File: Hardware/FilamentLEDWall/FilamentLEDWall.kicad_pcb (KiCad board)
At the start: 2 copper layers, 23 parts, among them U1 AMS1117-3.3, U2 AMS1117-5.0, U3 JXI5020GF

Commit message: updated circuit
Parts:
- removed C2: 10uF, Capacitor_SMD:C_0805_2012Metric_Pad1.15x1.40mm_HandSolder
- removed MOD1: ESP32-WROOM-32, digikey-footprints:ESP32-WROOM-32D
- removed U1: AMS1117-3.3, Package_TO_SOT_SMD:SOT-223-3_TabPin2
- removed U2: AMS1117-5.0, Package_TO_SOT_SMD:SOT-223-3_TabPin2
- added J1: TopLeftConnector, Connector_PinHeader_2.54mm:PinHeader_2x04_P2.54mm_Vertical_SMD, B.Cu at (81.8, 40.0)
- added J2: TopLeftConnector, Connector_PinHeader_2.54mm:PinHeader_2x04_P2.54mm_Vertical_SMD, B.Cu at (81.8, 145.0)
- added J3: TopLeftConnector, Connector_PinHeader_2.54mm:PinHeader_2x04_P2.54mm_Vertical_SMD, B.Cu at (186.8, 145.0)
- added J4: TopLeftConnector, Connector_PinHeader_2.54mm:PinHeader_2x04_P2.54mm_Vertical_SMD, B.Cu at (186.8, 40.0)
- C1, R1, U3: moved to B.Cu
- D1, D10, D11, D12, D13, D14, D15, D16, D2, D3, D4, D5, D6, D7, D8, D9: footprint LED_SMD:LED_0805_2012Metric_Pad1.15x1.40mm_HandSolder -> FilamentLEDWall:FilamentLED_30mm
- moved D13 104.1 mm to (90.8, 136.0), turned to 315 degrees
- moved D9 93.4 mm to (90.8, 107.0), turned to 225 degrees
- moved D15 69.0 mm to (148.8, 136.0), turned to 315 degrees
- moved D1 65.8 mm to (90.8, 49.0), turned to 225 degrees
- moved D5 64.2 mm to (90.8, 78.0), turned to 315 degrees
- moved D16 62.4 mm to (177.8, 136.0), turned to 45 degrees
- moved D14 58.0 mm to (119.8, 136.0), turned to 45 degrees
- moved R1 46.1 mm to (132.2, 87.0)
- moved D2 45.4 mm to (119.8, 49.0), turned to 135 degrees
- moved D12 41.9 mm to (177.8, 107.0), turned to 135 degrees
- moved D10 41.7 mm to (119.8, 107.0), turned to 135 degrees
- moved D6 41.5 mm to (119.8, 78.0), turned to 45 degrees
- moved D4 38.2 mm to (177.8, 49.0), turned to 135 degrees
- moved U3 35.2 mm to (134.2, 92.5), turned to 270 degrees
- moved D11 32.9 mm to (148.8, 107.0), turned to 225 degrees
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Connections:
- C1 pad 1: /3.3V_MCU -> /5V_LED
- U3 pad 22: (no net) -> LED_SDO
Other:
- board outline added: 116 x 116 mm
- rule pad_to_mask_clearance: 0.051 -> 0.05

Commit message: Updated light PCB v0.1
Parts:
- added C2: 100nF, Capacitor_SMD:C_0603_1608Metric_Pad1.05x0.95mm_HandSolder, B.Cu at (110.8, 67.1)
- C1: footprint Capacitor_SMD:C_0805_2012Metric_Pad1.15x1.40mm_HandSolder -> Capacitor_SMD:C_0603_1608Metric_Pad1.05x0.95mm_HandSolder
- J2: value TopLeftConnector -> BottomLeftConnector
- J3: value TopLeftConnector -> BottomRightConnector
- J4: value TopLeftConnector -> TopRightConnector
- R1: footprint Resistor_SMD:R_0805_2012Metric_Pad1.15x1.40mm_HandSolder -> Resistor_SMD:R_0603_1608Metric_Pad1.05x0.95mm_HandSolder
- moved U3 34.2 mm to (116.5, 63.3), turned to 0 degrees
- moved C1 30.8 mm to (110.8, 69.6), turned to 180 degrees
- moved J3 26.3 mm to (164.7, 130.6), turned to 180 degrees
- moved R1 25.7 mm to (113.3, 69.6), turned to 270 degrees
- moved D16 24.4 mm to (157.1, 123.0)
- moved D12 23.9 mm to (157.1, 95.0)
- moved J4 23.6 mm to (164.7, 31.5), turned to 270 degrees
- moved D15 23.5 mm to (129.2, 123.0)
- moved D8 23.3 mm to (157.1, 67.1)
- moved D11 22.9 mm to (129.2, 95.0)
- moved D4 22.9 mm to (157.1, 39.2)
- moved D14 22.6 mm to (101.2, 123.0)
- moved D7 22.4 mm to (129.2, 67.1)
- moved D10 22.0 mm to (101.2, 95.0)
- moved D3 21.9 mm to (129.2, 39.2)
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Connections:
- D1 pad 2: 5V -> /5V_LED
- D10 pad 2: 5V -> /5V_LED
- D11 pad 2: 5V -> /5V_LED
- D12 pad 2: 5V -> /5V_LED
- D13 pad 2: 5V -> /5V_LED
- D14 pad 2: 5V -> /5V_LED
- D15 pad 2: 5V -> /5V_LED
- D16 pad 2: 5V -> /5V_LED
- D2 pad 2: 5V -> /5V_LED
- D3 pad 2: 5V -> /5V_LED
- D4 pad 2: 5V -> /5V_LED
- D5 pad 2: 5V -> /5V_LED
- D6 pad 2: 5V -> /5V_LED
- D7 pad 2: 5V -> /5V_LED
- D8 pad 2: 5V -> /5V_LED
- D9 pad 2: 5V -> /5V_LED
- J1 pad 2: LED_CLK -> /5V_LED
- J1 pad 3: LED_LE -> LED_CLK
- J1 pad 4: LED_OE -> (no net)
- J1 pad 5: GND -> LED_LE
- J1 pad 7: LED_SDI -> LED_OE
- J1 pad 8: /5V_LED -> GND
- J2 pad 2: LED_CLK -> /5V_LED
- J2 pad 3: LED_LE -> LED_CLK
- J2 pad 4: LED_OE -> LED_SDI
- J2 pad 5: GND -> LED_LE
- J2 pad 6: LED_SDO -> (no net)
- J2 pad 7: LED_SDI -> LED_OE
- J2 pad 8: /5V_LED -> GND
- J3 pad 2: LED_CLK -> /5V_LED
- J3 pad 3: LED_LE -> LED_CLK
- J3 pad 4: LED_OE -> (no net)
- J3 pad 5: GND -> LED_LE
- J3 pad 7: LED_SDI -> LED_OE
- J3 pad 8: /5V_LED -> GND
- J4 pad 2: LED_CLK -> /5V_LED
- J4 pad 3: LED_LE -> LED_CLK
- J4 pad 4: LED_OE -> LED_SDI
- J4 pad 5: GND -> LED_LE
- J4 pad 6: LED_SDO -> (no net)
- J4 pad 7: LED_SDI -> LED_OE
- J4 pad 8: /5V_LED -> GND
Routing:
- net /5V_LED: track 0.00 -> 383.3 mm, vias 0 -> 2
- net LED_OE: track 0.00 -> 334.6 mm, vias 0 -> 18
- net LED_LE: track 0.00 -> 322.7 mm, vias 0 -> 16
- net LED_CLK: track 0.00 -> 317.5 mm, vias 0 -> 16
- net LED_SDI: track 0.00 -> 202.6 mm, vias 0 -> 14
- net LED_SDO: track 0.00 -> 195.4 mm, vias 0 -> 11
- net OUT12: track 0.00 -> 123.7 mm, vias 0 -> 2
- net OUT15: track 0.00 -> 120.5 mm, vias 0 -> 4
- net OUT0: track 0.00 -> 86.1 mm, vias 0 -> 2
- net OUT3: track 0.00 -> 84.3 mm, vias 0 -> 2
- net OUT8: track 0.00 -> 73.8 mm, vias 0 -> 4
- net OUT13: track 0.00 -> 72.4 mm, vias 0 -> 4
- net OUT14: track 0.00 -> 71.7 mm, vias 0 -> 4
- net OUT4: track 0.00 -> 70.5 mm, vias 0 -> 2
- net OUT11: track 0.00 -> 67.4 mm, vias 0 -> 2
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- added copper zone on B.Cu, net GND
- added copper zone on F.Cu, net GND
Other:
- board size 116 x 116 mm -> 113.8 x 113.8 mm
- board text added: "100nF"
- board text added: "10uF"
- board text added: "Filament Wall Cell v0.1 Sandbox Workshop Designed by Caorx Wangyw"
- board text added: "INPUT"
- board text added: "Iout=Vext(1.24V)/Rext*15"
- board text added: "OUTPUT"
- board text added: "R_EXT"

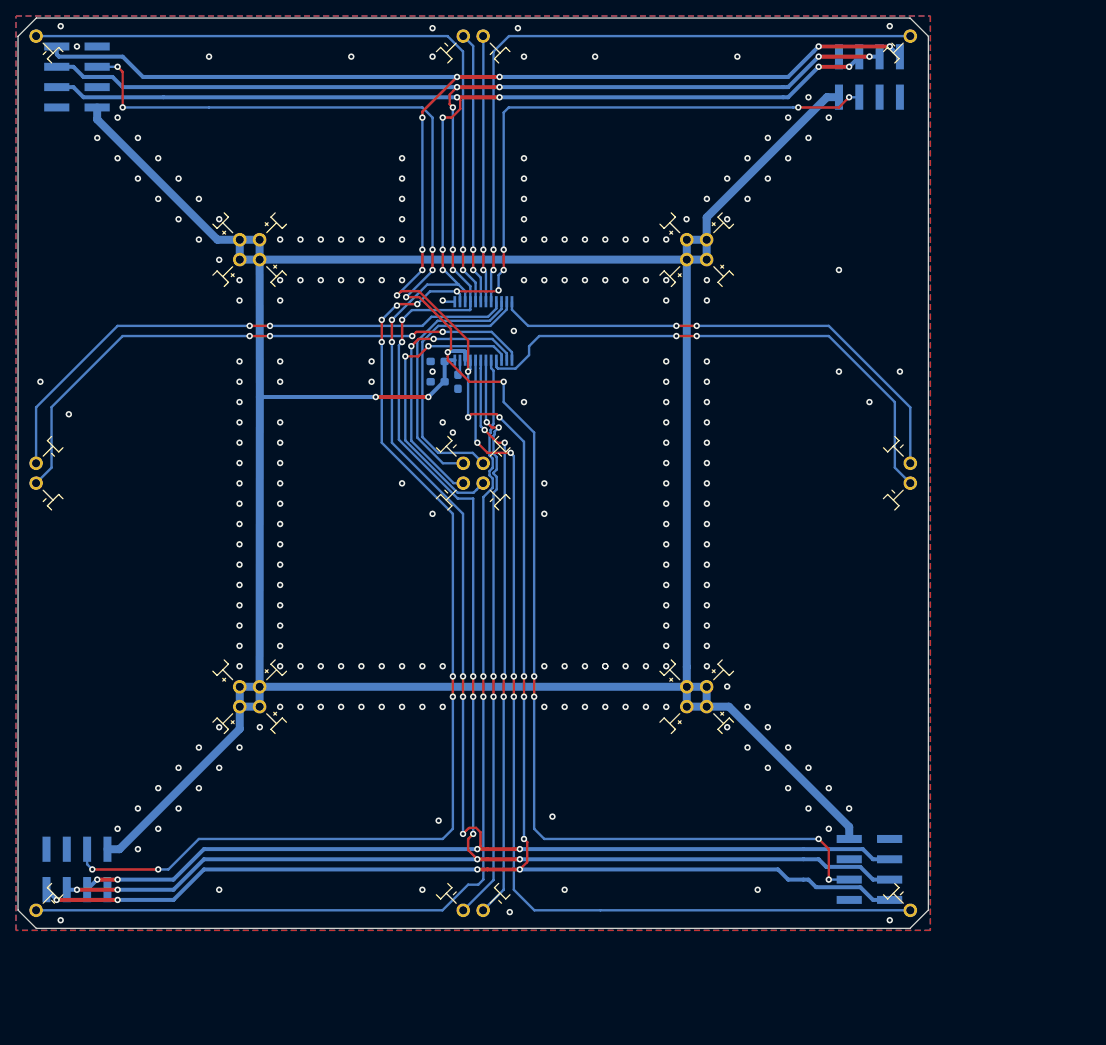
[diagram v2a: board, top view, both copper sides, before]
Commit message: Updated LED Board to v0.2
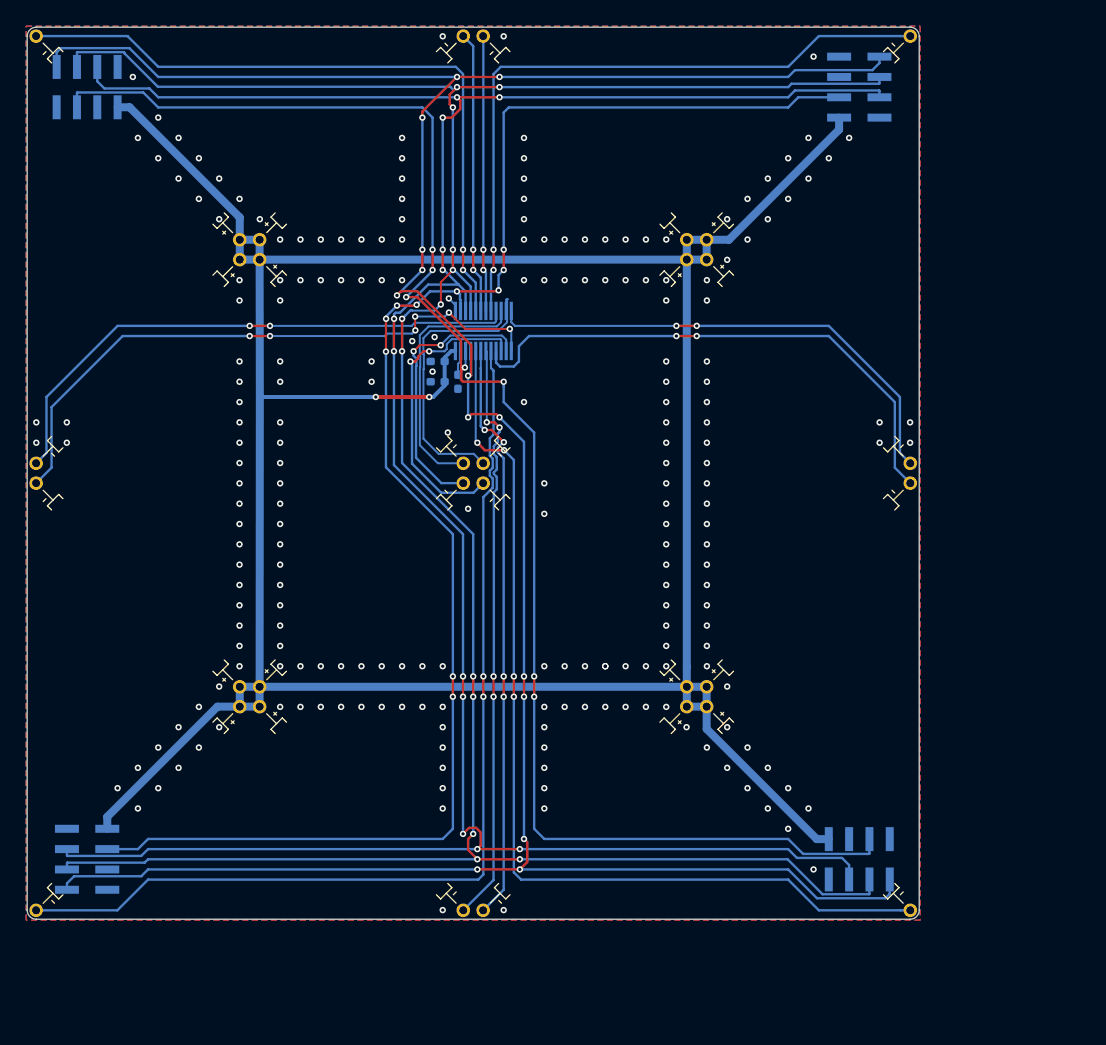
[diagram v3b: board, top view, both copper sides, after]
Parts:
- J1, J2, J3, J4: footprint Connector_PinHeader_2.54mm:PinHeader_2x04_P2.54mm_Vertical_SMD -> Connector_PinSocket_2.54mm:PinSocket_2x04_P2.54mm_Vertical_SMD
- U3: footprint Silicon-Standard:SSOP24 -> Sensor_Current:Allegro_QSOP-24_3.9x8.7mm_P0.635mm
- moved J1 1.80 mm to (66.9, 32.8), turned to 90 degrees
- moved J4 1.80 mm to (163.5, 32.8), turned to 0 degrees
- moved J2 1.80 mm to (66.9, 129.3), turned to 180 degrees
- moved J3 1.80 mm to (163.5, 129.3), turned to 270 degrees
- turned U3 to 270 degrees
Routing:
- net LED_SDI: track 202.6 -> 195.0 mm, vias 14 -> 10
- net /5V_LED: track 383.3 -> 377.5 mm
- net OUT8: track 73.8 -> 77.2 mm, vias 4 -> 6
- net OUT6: track 34.0 -> 37.2 mm
- net LED_SDO: track 195.4 -> 197.4 mm, vias 11 -> 7
- net OUT14: track 71.7 -> 73.3 mm
- net Net-(R1-Pad1): track 1.92 -> 3.46 mm
- net LED_CLK: track 317.5 -> 316.0 mm, vias 16 -> 12
- net OUT13: track 72.4 -> 73.8 mm
- net OUT1: track 34.1 -> 35.3 mm
- net OUT2: track 33.7 -> 34.9 mm
- net OUT11: track 67.4 -> 68.5 mm
- net OUT10: track 37.2 -> 38.2 mm
- net LED_OE: track 334.6 -> 333.7 mm, vias 18 -> 14
- net OUT12: track 123.7 -> 124.5 mm
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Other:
- board size 113.8 x 113.8 mm -> 111.5 x 111.5 mm
- board text added: "--"
- board text added: "5V"
- board text added: "CLK"
- board text added: "Filament Wall Cell v0.2 Sandbox Workshop Designed by Caorx Wangyw"
- board text added: "GND"
- board text added: "JLCJLCJLCJLC"
- board text added: "LE"
- board text added: "OE"
- board text added: "SDI"
- board text added: "SDO"
- board text removed: "Filament Wall Cell v0.1 Sandbox Workshop Designed by Caorx Wangyw"

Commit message: updated wall cell and connector
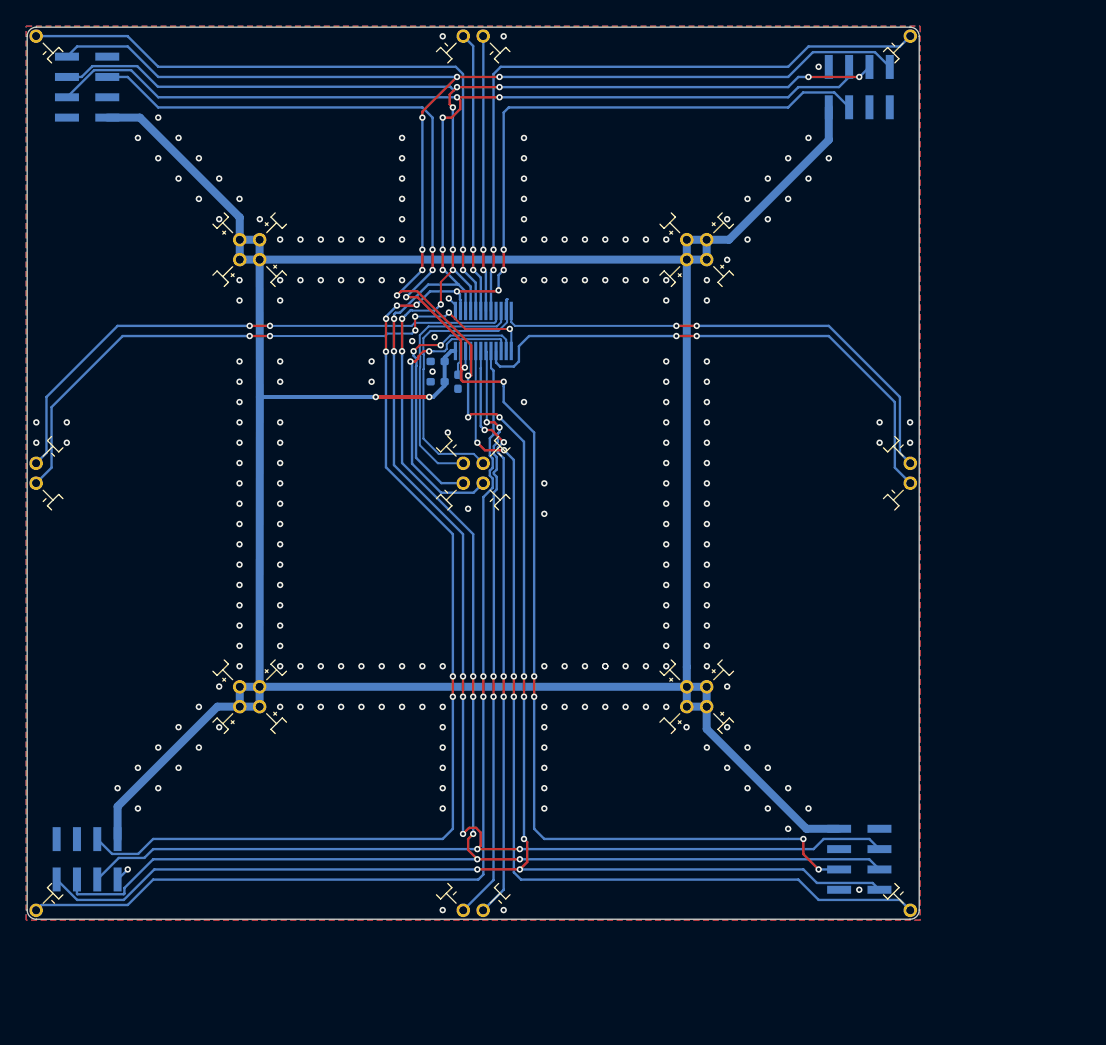
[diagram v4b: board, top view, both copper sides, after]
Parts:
- turned J1 to 0 degrees
- turned J2 to 90 degrees
- turned J3 to 180 degrees
- turned J4 to 270 degrees
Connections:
- J1 pad 1: GND -> /5V_LED
- J1 pad 2: /5V_LED -> GND
- J1 pad 3: LED_CLK -> Net-(J1-Pad3)
- J1 pad 4: (no net) -> LED_CLK
- J1 pad 5: LED_LE -> LED_SDO
- J1 pad 6: LED_SDO -> LED_LE
- J1 pad 7: LED_OE -> GND
- J1 pad 8: GND -> LED_OE
- J2 pad 1: GND -> /5V_LED
- J2 pad 2: /5V_LED -> GND
- J2 pad 3: LED_CLK -> LED_SDI
- J2 pad 4: LED_SDI -> LED_CLK
- J2 pad 5: LED_LE -> Net-(J2-Pad5)
- J2 pad 6: (no net) -> LED_LE
- J2 pad 7: LED_OE -> GND
- J2 pad 8: GND -> LED_OE
- J3 pad 1: GND -> /5V_LED
- J3 pad 2: /5V_LED -> GND
- J3 pad 3: LED_CLK -> Net-(J3-Pad3)
- J3 pad 4: (no net) -> LED_CLK
- J3 pad 5: LED_LE -> LED_SDO
- J3 pad 6: LED_SDO -> LED_LE
- J3 pad 7: LED_OE -> GND
- J3 pad 8: GND -> LED_OE
- J4 pad 1: GND -> /5V_LED
- J4 pad 2: /5V_LED -> GND
- J4 pad 3: LED_CLK -> LED_SDI
- J4 pad 4: LED_SDI -> LED_CLK
- J4 pad 5: LED_LE -> Net-(J4-Pad5)
- J4 pad 6: (no net) -> LED_LE
- J4 pad 7: LED_OE -> GND
- J4 pad 8: GND -> LED_OE
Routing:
- net LED_SDO: track 197.4 -> 188.9 mm, vias 7 -> 9
- net LED_SDI: track 195.0 -> 199.6 mm
- net GND: track 1.91 -> 4.94 mm, vias 222 -> 221
- net /5V_LED: track 377.5 -> 380.4 mm
- net LED_OE: track 333.7 -> 331.5 mm
- net LED_LE: track 322.3 -> 320.3 mm, vias 13 -> 15
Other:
- rule pad_to_mask_clearance: 0.05 -> 0
- board text added: "Filament Wall Cell v0.3 Sandbox Workshop Designed by Caorx Wangyw"
- board text removed: "Filament Wall Cell v0.2 Sandbox Workshop Designed by Caorx Wangyw"

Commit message: merged all
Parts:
- J1, J2, J3, J4: footprint Connector_PinSocket_2.54mm:PinSocket_2x04_P2.54mm_Vertical_SMD -> Connector_PinHeader_2.54mm:PinHeader_2x04_P2.54mm_Vertical_SMD
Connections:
- J1 pad 1: /5V_LED -> GND
- J1 pad 2: GND -> /5V_LED
- J1 pad 3: Net-(J1-Pad3) -> LED_CLK
- J1 pad 4: LED_CLK -> (no net)
- J1 pad 5: LED_SDO -> LED_LE
- J1 pad 6: LED_LE -> LED_SDO
- J1 pad 7: GND -> LED_OE
- J1 pad 8: LED_OE -> GND
- J2 pad 1: /5V_LED -> GND
- J2 pad 2: GND -> /5V_LED
- J2 pad 3: LED_SDI -> LED_CLK
- J2 pad 4: LED_CLK -> LED_SDI
- J2 pad 5: Net-(J2-Pad5) -> LED_LE
- J2 pad 6: LED_LE -> (no net)
- J2 pad 7: GND -> LED_OE
- J2 pad 8: LED_OE -> GND
- J3 pad 1: /5V_LED -> GND
- J3 pad 2: GND -> /5V_LED
- J3 pad 3: Net-(J3-Pad3) -> LED_CLK
- J3 pad 4: LED_CLK -> (no net)
- J3 pad 5: LED_SDO -> LED_LE
- J3 pad 6: LED_LE -> LED_SDO
- J3 pad 7: GND -> LED_OE
- J3 pad 8: LED_OE -> GND
- J4 pad 1: /5V_LED -> GND
- J4 pad 2: GND -> /5V_LED
- J4 pad 3: LED_SDI -> LED_CLK
- J4 pad 4: LED_CLK -> LED_SDI
- J4 pad 5: Net-(J4-Pad5) -> LED_LE
- J4 pad 6: LED_LE -> (no net)
- J4 pad 7: GND -> LED_OE
- J4 pad 8: LED_OE -> GND
